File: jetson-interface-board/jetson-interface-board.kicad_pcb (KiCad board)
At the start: 2 copper layers, 63 x 23 mm, 38 parts, among them J1 Conn_01x04, J2 Conn_01x04, J3 USB_C_Receptacle_USB2.0, J4 Conn_01x04, J5 Conn_01x18, U1 MCP2562-E-MF, U2 FT234XD, U3 XC8111AA01MR-G

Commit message: fix:[WIP]pin header
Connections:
- J5 pad 10: unconnected-(J5-Pin_10-Pad10) -> UART_RX
- J5 pad 11: GNDD -> unconnected-(J5-Pin_11-Pad11)
- J5 pad 15: CAN_TX -> +3.3V
- J5 pad 16: CAN_RX -> GNDD
- J5 pad 17: GNDD -> CAN_RX
- J5 pad 18: +3.3V -> CAN_TX
- J5 pad 2: unconnected-(J5-Pin_2-Pad2) -> GNDD
- J5 pad 3: UART_RX -> unconnected-(J5-Pin_3-Pad3)
- J5 pad 4: UART_TX -> GNDD
- J5 pad 6: unconnected-(J5-Pin_6-Pad6) -> GNDD
- J5 pad 7: GNDD -> unconnected-(J5-Pin_7-Pad7)
- J5 pad 9: GNDD -> UART_TX
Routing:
- net UART_RX: track 15.6 -> 0.00 mm
- net UART_TX: track 15.6 -> 0.00 mm
- net +3.3V: track 16.7 -> 9.84 mm
- net CAN_TX: track 4.31 -> 10.4 mm, vias 0 -> 1
- net CAN_RX: track 4.41 -> 6.50 mm
- net GNDD: vias 59 -> 60
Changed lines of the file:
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@@
 			(layers "*.Cu" "*.Mask")
 			(remove_unused_layers no)
-			(net "unconnected-(J5-Pin_2-Pad2)")
+			(net "GNDD")
 			(pinfunction "Pin_2_2")
-			(pintype "passive+no_connect")
+			(pintype "passive")
 		)
 		(pad "3" thru_hole oval
@@
 			(layers "*.Cu" "*.Mask")
 			(remove_unused_layers no)
-			(net "UART_RX")
+			(net "unconnected-(J5-Pin_3-Pad3)")
 			(pinfunction "Pin_3_3")
-			(pintype "passive")
+			(pintype "passive+no_connect")
 		)
 		(pad "4" thru_hole oval
@@
 			(layers "*.Cu" "*.Mask")
 			(remove_unused_layers no)
-			(net "UART_TX")
+			(net "GNDD")
 			(pinfunction "Pin_4_4")
 			(pintype "passive")
@@
 			(layers "*.Cu" "*.Mask")
 			(remove_unused_layers no)
-			(net "unconnected-(J5-Pin_6-Pad6)")
+			(net "GNDD")
 			(pinfunction "Pin_6_6")
-			(pintype "passive+no_connect")
+			(pintype "passive")
 		)
 		(pad "7" thru_hole oval
@@
 			(layers "*.Cu" "*.Mask")
 			(remove_unused_layers no)
-			(net "GNDD")
+			(net "unconnected-(J5-Pin_7-Pad7)")
 			(pinfunction "Pin_7_7")
-			(pintype "passive")
+			(pintype "passive+no_connect")
 		)
 		(pad "8" thru_hole oval
@@
 			(layers "*.Cu" "*.Mask")
 			(remove_unused_layers no)
-			(net "GNDD")
+			(net "UART_TX")
 			(pinfunction "Pin_9_9")
 			(pintype "passive")
@@
 			(layers "*.Cu" "*.Mask")
 			(remove_unused_layers no)
-			(net "unconnected-(J5-Pin_10-Pad10)")
+			(net "UART_RX")
 			(pinfunction "Pin_10_10")
-			(pintype "passive+no_connect")
+			(pintype "passive")
 		)
 		(pad "11" thru_hole oval
@@
 			(layers "*.Cu" "*.Mask")
 			(remove_unused_layers no)
-			(net "GNDD")
+			(net "unconnected-(J5-Pin_11-Pad11)")
 			(pinfunction "Pin_11_11")
-			(pintype "passive")
+			(pintype "passive+no_connect")
 		)
 		(pad "12" thru_hole oval
@@
 			(layers "*.Cu" "*.Mask")
 			(remove_unused_layers no)
-			(net "CAN_TX")
+			(net "+3.3V")
 			(pinfunction "Pin_15_15")
 			(pintype "passive")
@@
 			(layers "*.Cu" "*.Mask")
 			(remove_unused_layers no)
-			(net "CAN_RX")
+			(net "GNDD")
 			(pinfunction "Pin_16_16")
 			(pintype "passive")
@@
 			(layers "*.Cu" "*.Mask")
 			(remove_unused_layers no)
-			(net "GNDD")
+			(net "CAN_RX")
 			(pinfunction "Pin_17_17")
 			(pintype "passive")
@@
 			(layers "*.Cu" "*.Mask")
 			(remove_unused_layers no)
-			(net "+3.3V")
+			(net "CAN_TX")
 			(pinfunction "Pin_18_18")
 			(pintype "passive")
@@
 	)
 	(via
+		(at 29.3 20.5)
+		(size 0.6)
+		(drill 0.3)
+		(layers "F.Cu" "B.Cu")
+		(free yes)
+		(net "GNDD")
+	)
+	(via
 		(at 33.6 20.8)
 		(size 0.6)
@@
 	)
 	(via
-		(at 29.2 20)
+		(at 28.5 19.1)
 		(size 0.6)
 		(drill 0.3)
@@
 	)
 	(segment
-		(start 68.725 27.775)
-		(end 68.725 22.525)
-		(width 0.2)
-		(layer "F.Cu")
-		(net "UART_RX")
-	)
-	(segment
-		(start 67.4 21.2)
-		(end 64.2 21.2)
-		(width 0.2)
-		(layer "F.Cu")
-		(net "UART_RX")
-	)
-	(segment
-		(start 68.725 22.525)
-		(end 67.4 21.2)
-		(width 0.2)
-		(layer "F.Cu")
-		(net "UART_RX")
-	)
-	(segment
-		(start 64.2 21.2)
-		(end 62.96 19.96)
-		(width 0.2)
-		(layer "F.Cu")
-		(net "UART_RX")
-	)
-	(segment
-		(start 62.96 19.96)
-		(end 62.96 16.4)
-		(width 0.2)
+		(start 31.283884 17.6)
+		(end 32.3 18.616116)
+		(width 0.25)
 		(layer "F.Cu")
-		(net "UART_RX")
+		(net "CAN_TX")
 	)
 	(segment
-		(start 67.375 27.775)
-		(end 67.375 26.941722)
-		(width 0.2)
+		(start 30.926686 17.6)
+		(end 31.283884 17.6)
+		(width 0.25)
 		(layer "F.Cu")
-		(net "UART_TX")
+		(net "CAN_TX")
 	)
 	(segment
-		(start 61.8 23.6)
-		(end 60.42 22.22)
-		(width 0.2)
+		(start 32.3 18.616116)
+		(end 32.3 20.6375)
+		(width 0.25)
 		(layer "F.Cu")
-		(net "UART_TX")
+		(net "CAN_TX")
 	)
 	(segment
-		(start 67.375 26.941722)
-		(end 64.033278 23.6)
-		(width 0.2)
+		(start 30.883988 17.557302)
+		(end 30.926686 17.6)
+		(width 0.25)
 		(layer "F.Cu")
-		(net "UART_TX")
+		(net "CAN_TX")
 	)
-	(segment
-		(start 64.033278 23.6)
-		(end 61.8 23.6)
-		(width 0.2)
-		(layer "F.Cu")
-		(net "UART_TX")
+	(via
+		(at 30.883988 17.557302)
+		(size 0.6)
+		(drill 0.3)
+		(layers "F.Cu" "B.Cu")
+		(net "CAN_TX")
 	)
 	(segment
-		(start 60.42 22.22)
-		(end 60.42 16.4)
-		(width 0.2)
-		(layer "F.Cu")
-		(net "UART_TX")
+		(start 30.84129 17.6)
+		(end 26.06 17.6)
+		(width 0.25)
+		(layer "B.Cu")
+		(net "CAN_TX")
 	)
 	(segment
-		(start 32.3 16.58)
-		(end 32.48 16.4)
+		(start 26.06 17.6)
+		(end 24.86 16.4)
 		(width 0.25)
-		(layer "F.Cu")
+		(layer "B.Cu")
 		(net "CAN_TX")
 	)
 	(segment
-		(start 32.3 20.6375)
-		(end 32.3 16.58)
+		(start 30.883988 17.557302)
+		(end 30.84129 17.6)
 		(width 0.25)
-		(layer "F.Cu")
+		(layer "B.Cu")
 		(net "CAN_TX")
 	)
 	(segment
-		(start 30.35 19.75)
-		(end 30.2 19.6)
+		(start 28.116116 19.8)
+		(end 27.4 19.083884)
 		(width 0.25)
 		(layer "F.Cu")
@@
 	(segment
 		(start 30.35 20.6375)
-		(end 30.35 19.75)
+		(end 30.35 20.25)
 		(width 0.25)
 		(layer "F.Cu")
@@
 	)
 	(segment
-		(start 30.2 16.66)
-		(end 29.94 16.4)
+		(start 30.35 20.25)
+		(end 29.9 19.8)
 		(width 0.25)
 		(layer "F.Cu")
@@
 	)
 	(segment
-		(start 30.2 19.6)
-		(end 30.2 16.66)
+		(start 29.9 19.8)
+		(end 28.116116 19.8)
 		(width 0.25)
 		(layer "F.Cu")
@@
 	)
 	(segment
-		(start 23 22.5125)
-		(end 23 18.26)
+		(start 27.4 19.083884)
+		(end 27.4 16.4)
 		(width 0.25)
 		(layer "F.Cu")
-		(net "+3.3V")
+		(net "CAN_RX")
 	)
 	(segment
@@
 		(layer "F.Cu")
 		(net "+3.3V")
-	)
-	(segment
-		(start 23 18.26)
-		(end 24.86 16.4)
-		(width 0.25)
-		(layer "F.Cu")
-		(net "+3.3V")

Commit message: feat:route all nets
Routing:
- net UART_RX: track 0.00 -> 30.5 mm
- net UART_TX: track 0.00 -> 24.6 mm, vias 0 -> 1
- net +3.3V: track 9.84 -> 18.6 mm, vias 0 -> 1
- net +5V: track 43.8 -> 40.3 mm
- net CAN_TX: track 10.4 -> 10.2 mm, vias 1 -> 0
- net CAN_RX: track 6.50 -> 6.41 mm, vias 0 -> 1
- net GNDD: vias 60 -> 64

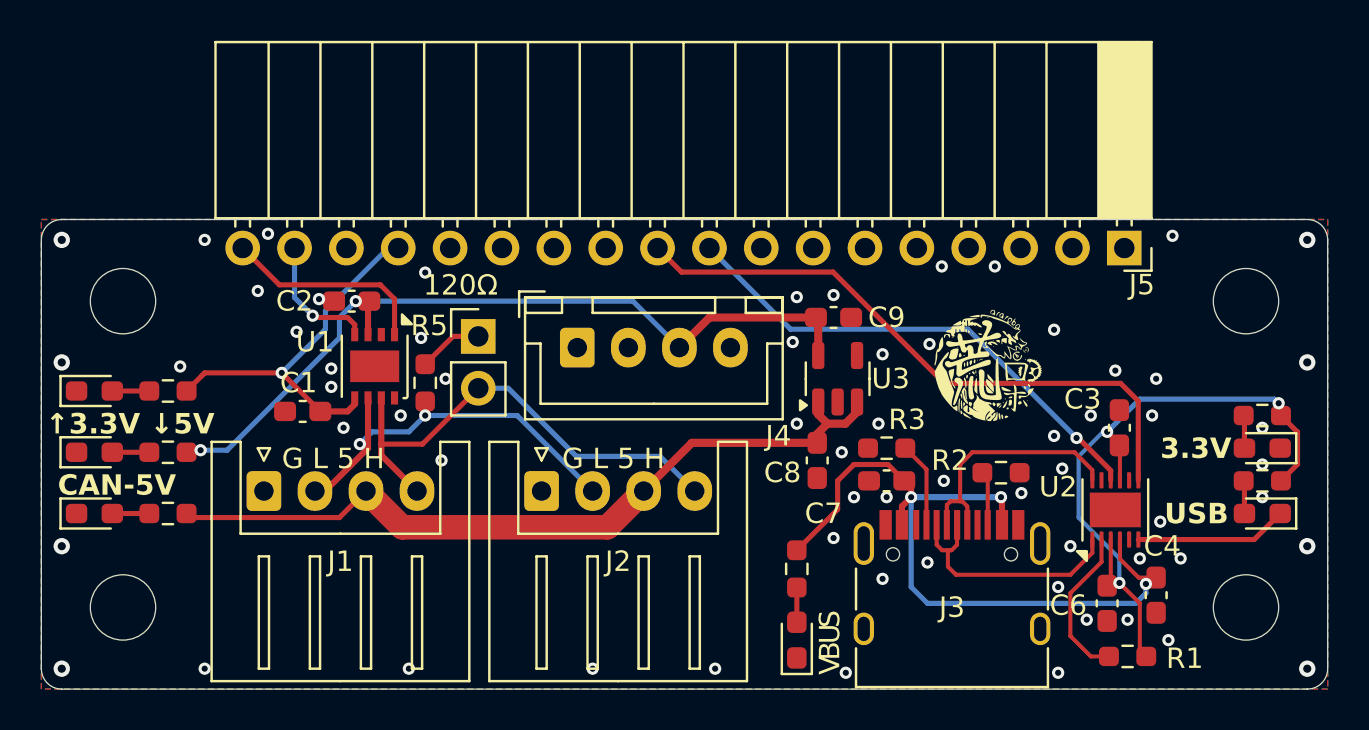
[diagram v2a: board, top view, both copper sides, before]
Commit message: 配線修正 ガーバー出力
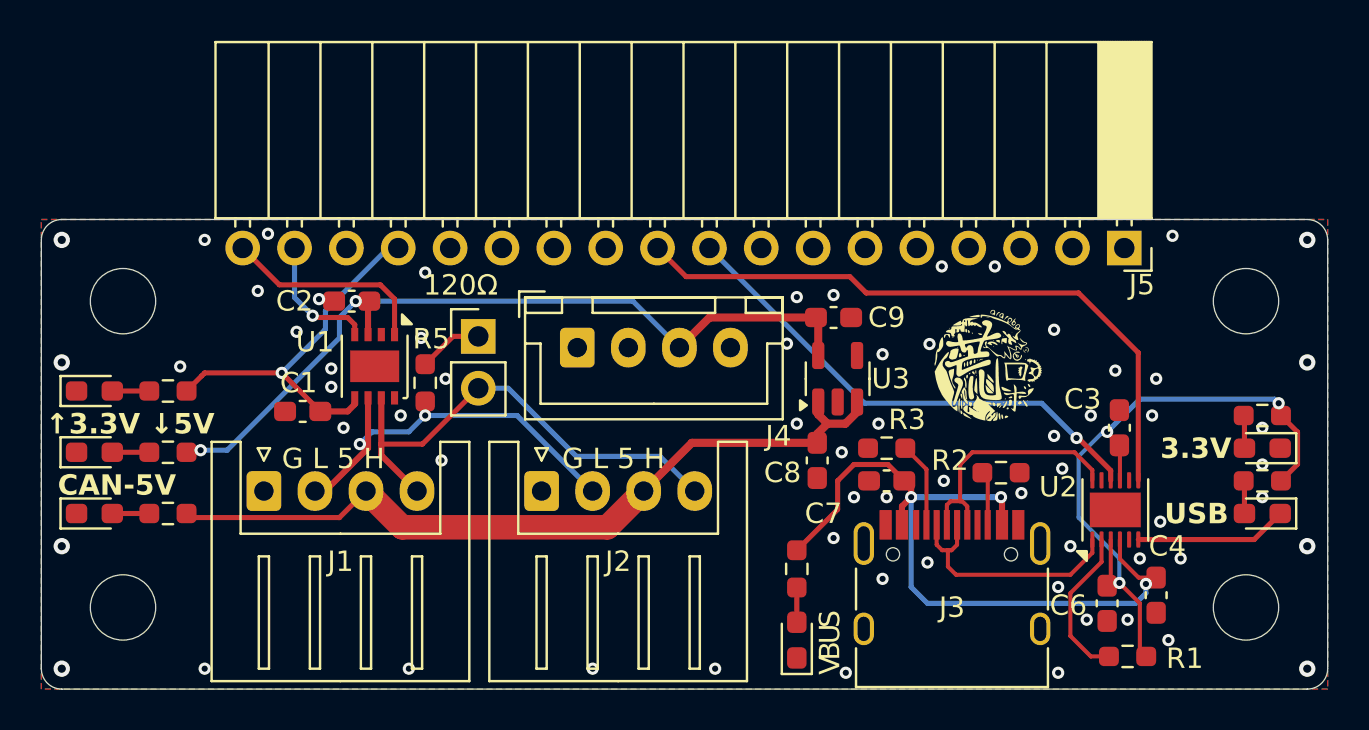
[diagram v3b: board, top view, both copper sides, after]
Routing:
- net UART_RX: track 30.5 -> 31.9 mm
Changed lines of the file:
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@@
 		(tags "resistor handsolder")
 		(property "Reference" "R5"
-			(at -2.8 -0.2 180)
+			(at -2.15 -0.3 180)
 			(layer "F.SilkS")
 			(effects
@@
 		(tags "capacitor handsolder")
 		(property "Reference" "C4"
-			(at -2.4 -0.3 180)
+			(at -2.4 -0.55 180)
 			(layer "F.SilkS")
 			(effects
@@
 	)
 	(via
-		(at 51.8 21)
+		(at 51.518058 21.081942)
 		(size 0.6)
 		(drill 0.3)
@@
 	)
 	(segment
-		(start 51.695 20.375)
-		(end 47.72 16.4)
+		(start 65.7 25.7)
+		(end 64 24)
 		(width 0.25)
 		(layer "B.Cu")
@@
 	)
 	(segment
-		(start 65.7 25.7)
-		(end 60.375 20.375)
+		(start 55.32 24)
+		(end 47.72 16.4)
 		(width 0.25)
 		(layer "B.Cu")
@@
 	)
 	(segment
-		(start 60.375 20.375)
-		(end 51.695 20.375)
+		(start 64 24)
+		(end 55.32 24)
 		(width 0.25)
 		(layer "B.Cu")
@@
 	)
 	(segment
-		(start 68.725 27.775)
-		(end 68.725 23.891116)
+		(start 54.6 17.8)
+		(end 46.58 17.8)
 		(width 0.25)
 		(layer "F.Cu")
@@
 	)
 	(segment
-		(start 67.858884 23.025)
-		(end 59.227076 23.025)
+		(start 68.725 21.525)
+		(end 65.8 18.6)
 		(width 0.25)
 		(layer "F.Cu")
@@
 	)
 	(segment
-		(start 68.725 23.891116)
-		(end 67.858884 23.025)
+		(start 55.4 18.6)
+		(end 54.6 17.8)
 		(width 0.25)
 		(layer "F.Cu")
@@
 	)
 	(segment
-		(start 53.777076 17.575)
-		(end 46.355 17.575)
+		(start 65.8 18.6)
+		(end 55.4 18.6)
 		(width 0.25)
 		(layer "F.Cu")
@@
 	)
 	(segment
-		(start 46.355 17.575)
-		(end 45.18 16.4)
+		(start 68.725 27.775)
+		(end 68.725 21.525)
 		(width 0.25)
 		(layer "F.Cu")
@@
 	)
 	(segment
-		(start 59.227076 23.025)
-		(end 53.777076 17.575)
+		(start 46.58 17.8)
+		(end 45.18 16.4)
 		(width 0.25)
 		(layer "F.Cu")
